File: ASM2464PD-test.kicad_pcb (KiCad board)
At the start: 2 copper layers, 34.6 x 22 mm, 19 parts, among them J1 USB_C_Receptacle, J2 Bus_M.2_Socket_M

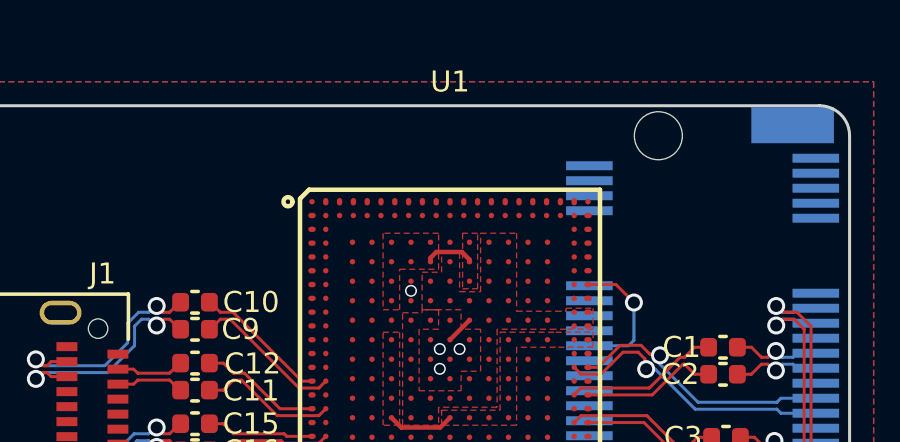
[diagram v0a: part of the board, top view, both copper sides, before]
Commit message: Labeled power rails, upgraded to KiCad 8
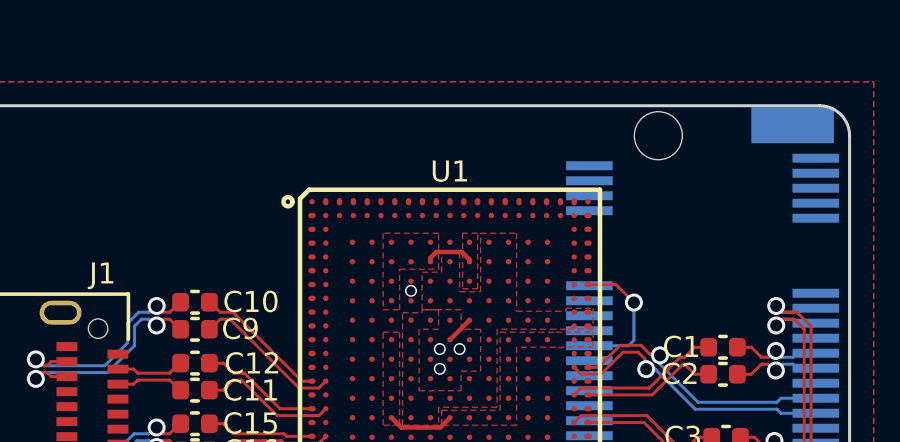
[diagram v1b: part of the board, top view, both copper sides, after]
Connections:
- net VCCH renamed 3.3V
- net VCCL renamed 1.8V
- net VDD renamed 1.05V
- U1 pad H5: unconnected-(U1C-VCCA33-PadH5) -> 3.3VA

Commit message: Updated symbol to match reference schematic
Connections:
- net 1.05V renamed 0.95V
- U1 pad G21: PERST# -> unconnected-(U1A-PERST0#-PadG21)

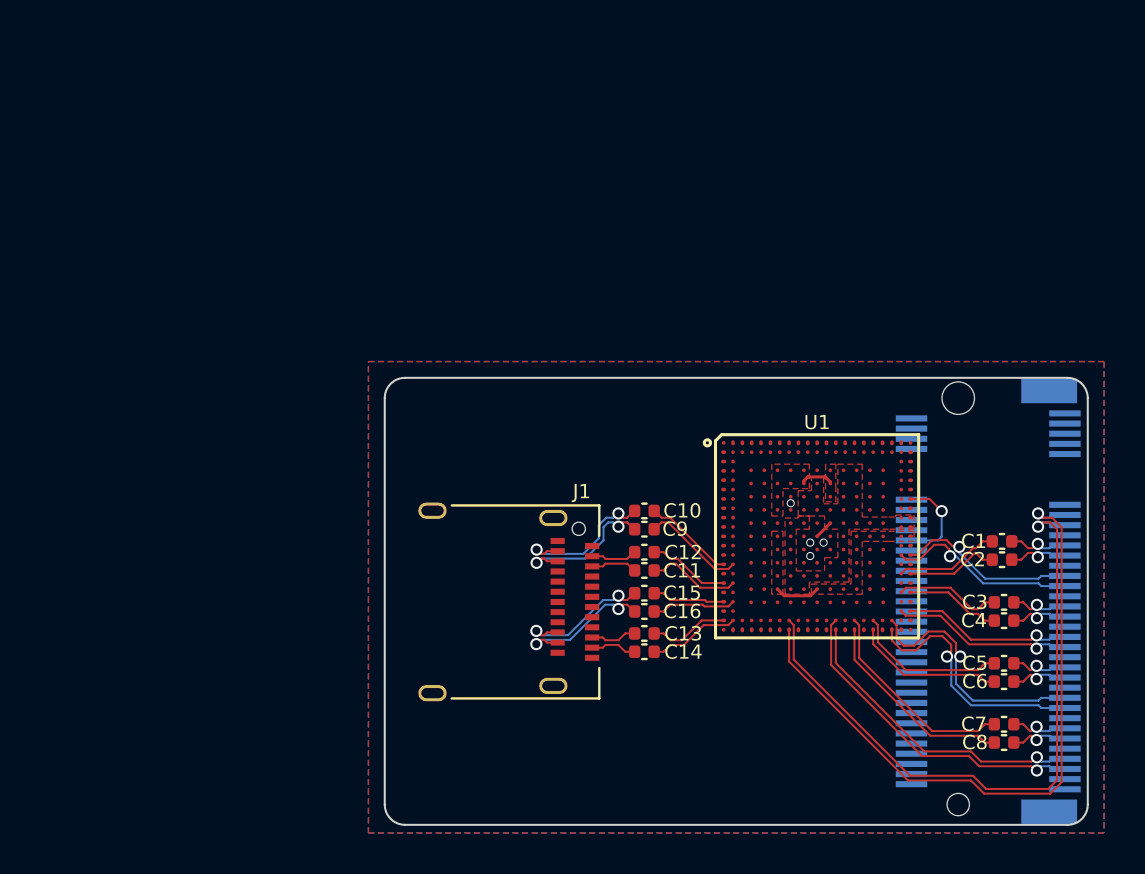
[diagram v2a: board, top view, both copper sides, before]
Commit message: Updated schematic and rerouted some stuff
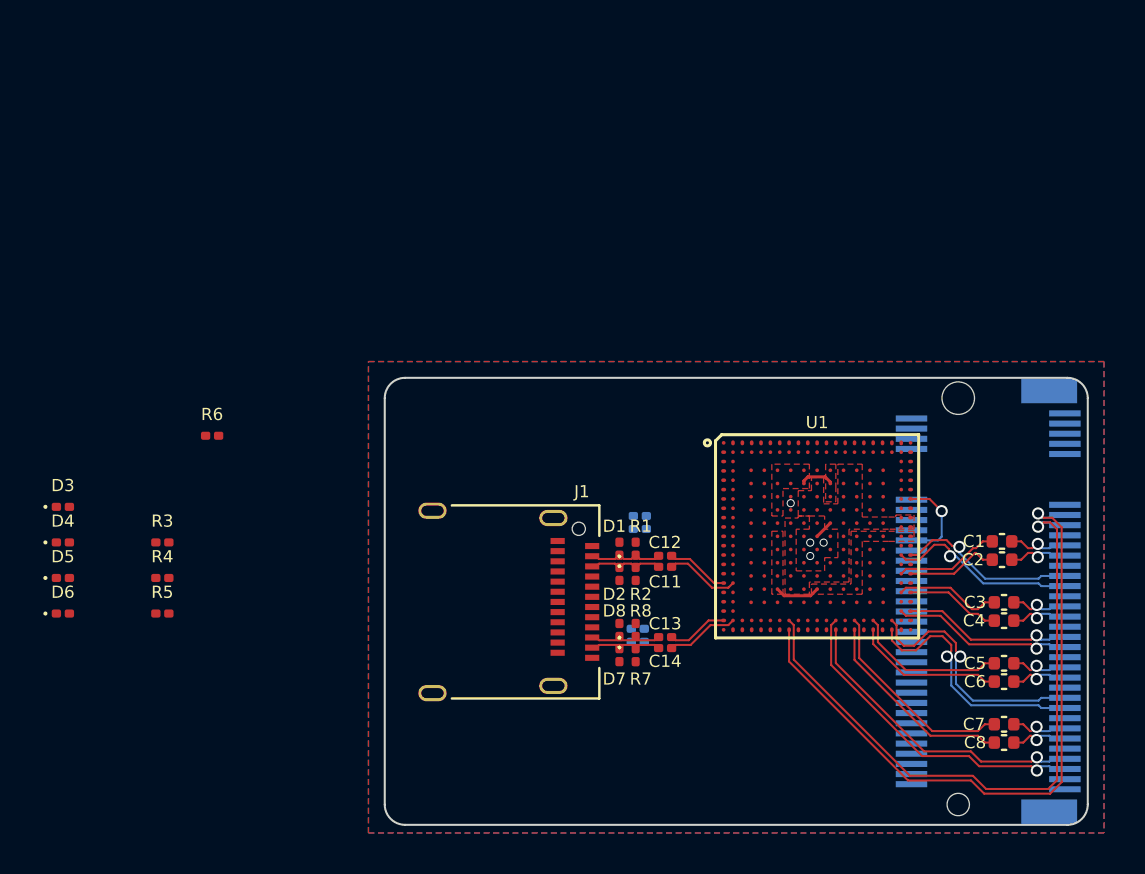
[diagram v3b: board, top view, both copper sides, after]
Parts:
- added D1: ~, Diode_SMD:D_0201_0603Metric, F.Cu at (57.0, 78.4)
- added D2: ~, Diode_SMD:D_0201_0603Metric, F.Cu at (57.0, 79.7)
- added D3: ~, Diode_SMD:D_0201_0603Metric, F.Cu at (29.6, 76.3)
- added D4: ~, Diode_SMD:D_0201_0603Metric, F.Cu at (29.6, 78.1)
- added D5: ~, Diode_SMD:D_0201_0603Metric, F.Cu at (29.6, 79.8)
- added D6: ~, Diode_SMD:D_0201_0603Metric, F.Cu at (29.6, 81.6)
- added D7: ~, Diode_SMD:D_0201_0603Metric, F.Cu at (57.0, 83.6)
- added D8: ~, Diode_SMD:D_0201_0603Metric, F.Cu at (57.0, 82.4)
- added R1: 220k, Resistor_SMD:R_0201_0603Metric, F.Cu at (57.8, 78.4)
- added R2: 220k, Resistor_SMD:R_0201_0603Metric, F.Cu at (57.8, 79.7)
- added R3: 220k, Resistor_SMD:R_0201_0603Metric, F.Cu at (34.5, 78.1)
- added R4: 220k, Resistor_SMD:R_0201_0603Metric, F.Cu at (34.5, 79.8)
- added R5: 220k, Resistor_SMD:R_0201_0603Metric, F.Cu at (34.5, 81.6)
- added R6: 220k, Resistor_SMD:R_0201_0603Metric, F.Cu at (36.9, 72.8)
- added R7: 220k, Resistor_SMD:R_0201_0603Metric, F.Cu at (57.8, 83.7)
- added R8: 220k, Resistor_SMD:R_0201_0603Metric, F.Cu at (57.8, 82.4)
- C10, C15, C16, C9: value 0.22u -> 0.33u; footprint Capacitor_SMD:C_0402_1005Metric -> Capacitor_SMD:C_0201_0603Metric; moved to B.Cu
- C11, C12, C13, C14: value 0.22u -> 0.33u; footprint Capacitor_SMD:C_0402_1005Metric -> Capacitor_SMD:C_0201_0603Metric
- moved C15 1.78 mm to (57.9, 82.3)
- moved C16 1.53 mm to (57.9, 83.0)
- moved C11 1.04 mm to (59.2, 79.3)
- moved C12 1.04 mm to (59.2, 78.8)
- moved C13 1.04 mm to (59.2, 82.8)
- moved C14 1.04 mm to (59.2, 83.3)
- moved C10 0.34 mm to (58.0, 76.8)
- moved C9 0.23 mm to (58.0, 77.4)
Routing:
- net /URX0_C-: track 7.52 -> 0.00 mm, vias 2 -> 0
- net /URX0_C+: track 7.52 -> 0.00 mm, vias 2 -> 0
- net /UTX1_C-: track 7.15 -> 0.00 mm, vias 2 -> 0
- net /UTX1_C+: track 7.15 -> 0.00 mm, vias 2 -> 0
- net URX0-: track 5.06 -> 0.00 mm
- net URX0+: track 4.51 -> 0.00 mm
- net UTX1+: track 4.15 -> 0.00 mm
- net UTX1-: track 3.59 -> 0.00 mm
- net /UTX0_C-: track 2.28 -> 3.70 mm
- net /UTX0_C+: track 2.28 -> 3.70 mm
- net /URX1_C-: track 2.28 -> 3.39 mm
- net /URX1_C+: track 2.28 -> 3.39 mm
- net URX1-: track 3.96 -> 3.03 mm
- net UTX0-: track 4.60 -> 3.67 mm
- net URX1+: track 4.52 -> 3.58 mm
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
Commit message: Added SPI flash, probably some more stuff, and made pcb 4-layer
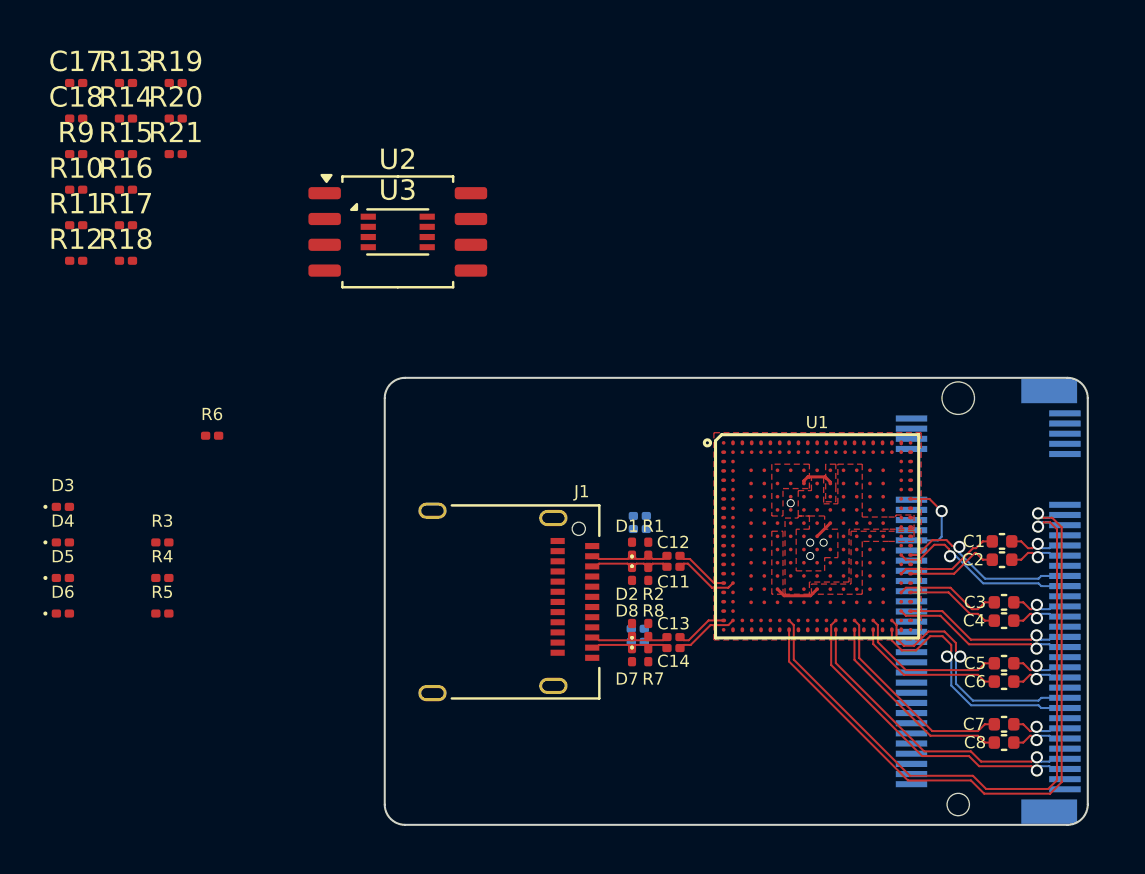
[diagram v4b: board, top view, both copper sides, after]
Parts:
- added C17: 1u, Capacitor_SMD:C_0201_0603Metric, F.Cu at (30.2, 55.5)
- added C18: 0.1u, Capacitor_SMD:C_0201_0603Metric, F.Cu at (30.2, 57.2)
- added R10: 0Ω, Resistor_SMD:R_0201_0603Metric, F.Cu at (30.2, 60.7)
- added R11: 0Ω, Resistor_SMD:R_0201_0603Metric, F.Cu at (30.2, 62.5)
- added R12: 0Ω, Resistor_SMD:R_0201_0603Metric, F.Cu at (30.2, 64.2)
- added R13: 0Ω, Resistor_SMD:R_0201_0603Metric, F.Cu at (32.7, 55.5)
- added R14: 0Ω, Resistor_SMD:R_0201_0603Metric, F.Cu at (32.7, 57.2)
- added R15: 4.7k, Resistor_SMD:R_0201_0603Metric, F.Cu at (32.7, 59.0)
- added R16: 10k, Resistor_SMD:R_0201_0603Metric, F.Cu at (32.7, 60.7)
- added R17: 4.7k, Resistor_SMD:R_0201_0603Metric, F.Cu at (32.7, 62.5)
- added R18: 4.7k, Resistor_SMD:R_0201_0603Metric, F.Cu at (32.7, 64.2)
- added R19: 0Ω, Resistor_SMD:R_0201_0603Metric, F.Cu at (35.1, 55.5)
- added R20: 0Ω, Resistor_SMD:R_0201_0603Metric, F.Cu at (35.1, 57.2)
- added R21: 0Ω, Resistor_SMD:R_0201_0603Metric, F.Cu at (35.1, 59.0)
- added R9: 0Ω, Resistor_SMD:R_0201_0603Metric, F.Cu at (30.2, 59.0)
- added U2: SPI_SOIC-8, Package_SO:SOIC-8_5.23x5.23mm_P1.27mm, F.Cu at (46.0, 62.8)
- added U3: SPI_DFN-8, Package_DFN_QFN:DFN-8-1EP_3x2mm_P0.5mm_EP1.3x1.5mm, F.Cu at (46.0, 62.8)
- moved D7 0.62 mm to (57.6, 83.7)
- moved D1 0.62 mm to (57.6, 78.4)
- moved D2 0.62 mm to (57.6, 79.7)
- moved D8 0.62 mm to (57.6, 82.4)
- moved R1 0.62 mm to (58.4, 78.4)
- moved R2 0.62 mm to (58.4, 79.7)
- moved R7 0.62 mm to (58.4, 83.7)
- moved R8 0.62 mm to (58.4, 82.4)
- moved C11 0.41 mm to (59.6, 79.3)
- moved C12 0.41 mm to (59.6, 78.8)
- moved C13 0.41 mm to (59.6, 82.8)
- moved C14 0.41 mm to (59.6, 83.3)
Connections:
- net 3.3V renamed +3.3V
- net 3.3VA renamed +3.3VA
- net Net-(J1-VBUS-PadA4) renamed +5V_VBUS
- J1 pad A5: CC1 -> /CC1_C
- J1 pad A6: USB2_D+ -> /USB2_C_D+
- J1 pad A7: USB2_D- -> /USB2_C_D-
- J1 pad A8: SBU1 -> /SBU1_C
- J1 pad B5: CC2 -> /CC2_C
- J1 pad B6: USB2_D+ -> /USB2_C_D+
- J1 pad B7: USB2_D- -> /USB2_C_D-
- J1 pad B8: SBU2 -> /SBU2_C
- J2 pad 50: PERST# -> Net-(J2-~{PERST})
- J2 pad 52: unconnected-(J2-~{CLKREQ}-Pad52) -> Net-(J2-~{CLKREQ})
- J2 pad 54: unconnected-(J2-~{PEWAKE}-Pad54) -> Net-(J2-~{PEWAKE})
- U1 pad A2: unconnected-(U1A-SPI_CS#-PadA2) -> SPI_CS#
- U1 pad A3: unconnected-(U1A-SPI_DO-PadA3) -> SPI_DO
- U1 pad A4: unconnected-(U1A-SPI_DI-PadA4) -> SPI_DI
- U1 pad A5: unconnected-(U1A-SPI_CLK-PadA5) -> SPI_CLK
- U1 pad G1: unconnected-(U1A-VBUS-PadG1) -> VBUS
- U1 pad G21: unconnected-(U1A-PERST0#-PadG21) -> PERST#
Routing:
- added copper zone on In1.Cu, net GND
- added copper zone on In2.Cu, net GND
- removed copper zone on B.Cu, net GND
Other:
- copper layers 2 -> 4

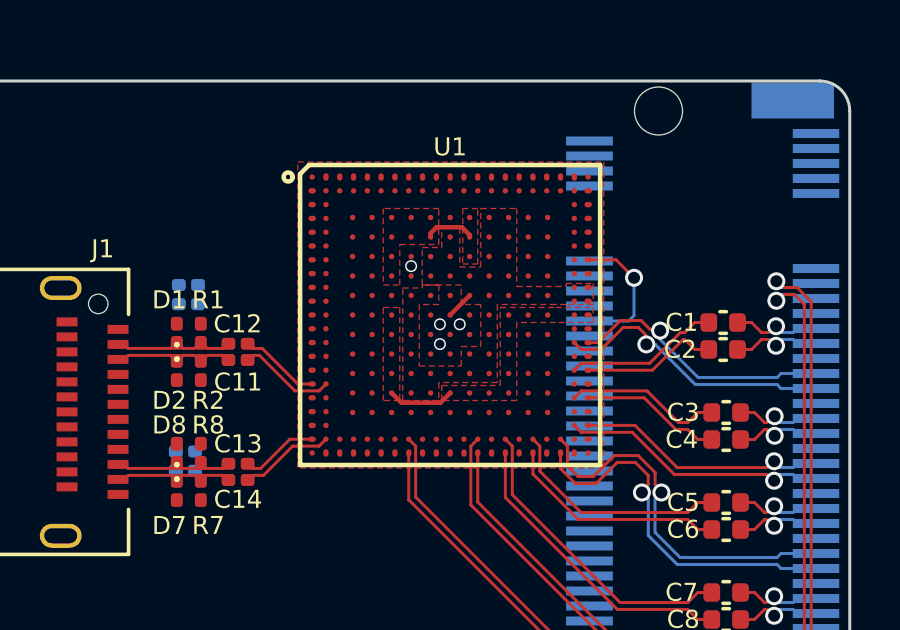
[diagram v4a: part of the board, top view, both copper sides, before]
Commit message: Added lots of power rail vias under chip
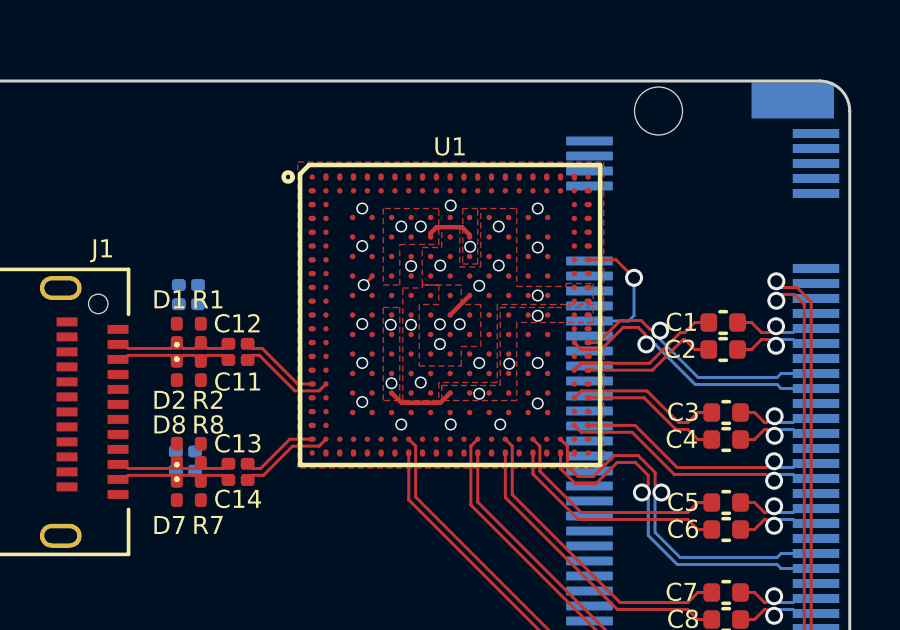
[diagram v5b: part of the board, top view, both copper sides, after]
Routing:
- net +3.3VA: track 0.00 -> 0.42 mm, vias 0 -> 1
- net GND: vias 4 -> 17
- net 1.8V: vias 0 -> 5
- net 0.95V: vias 0 -> 8
- net +3.3V: vias 0 -> 3

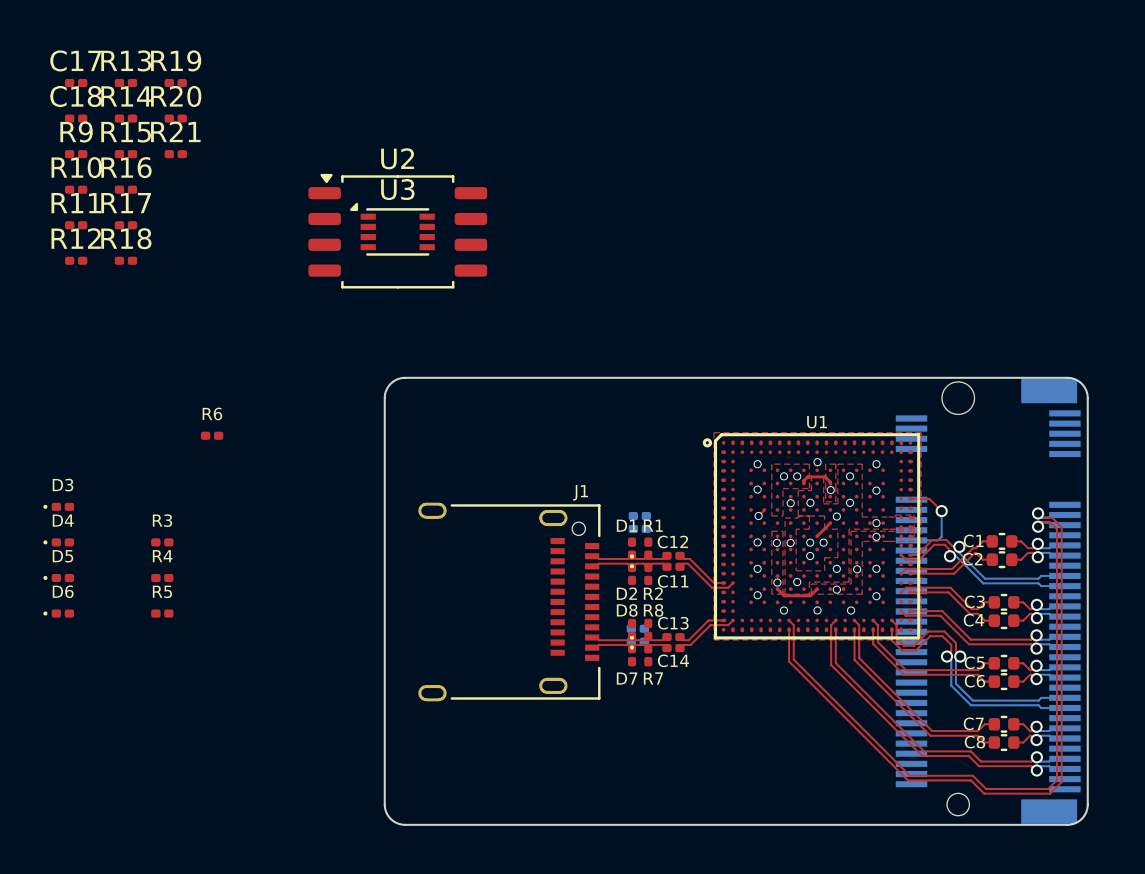
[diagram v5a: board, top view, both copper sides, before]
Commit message: reran the other 2 USB4 pairs too, placed esd stuff
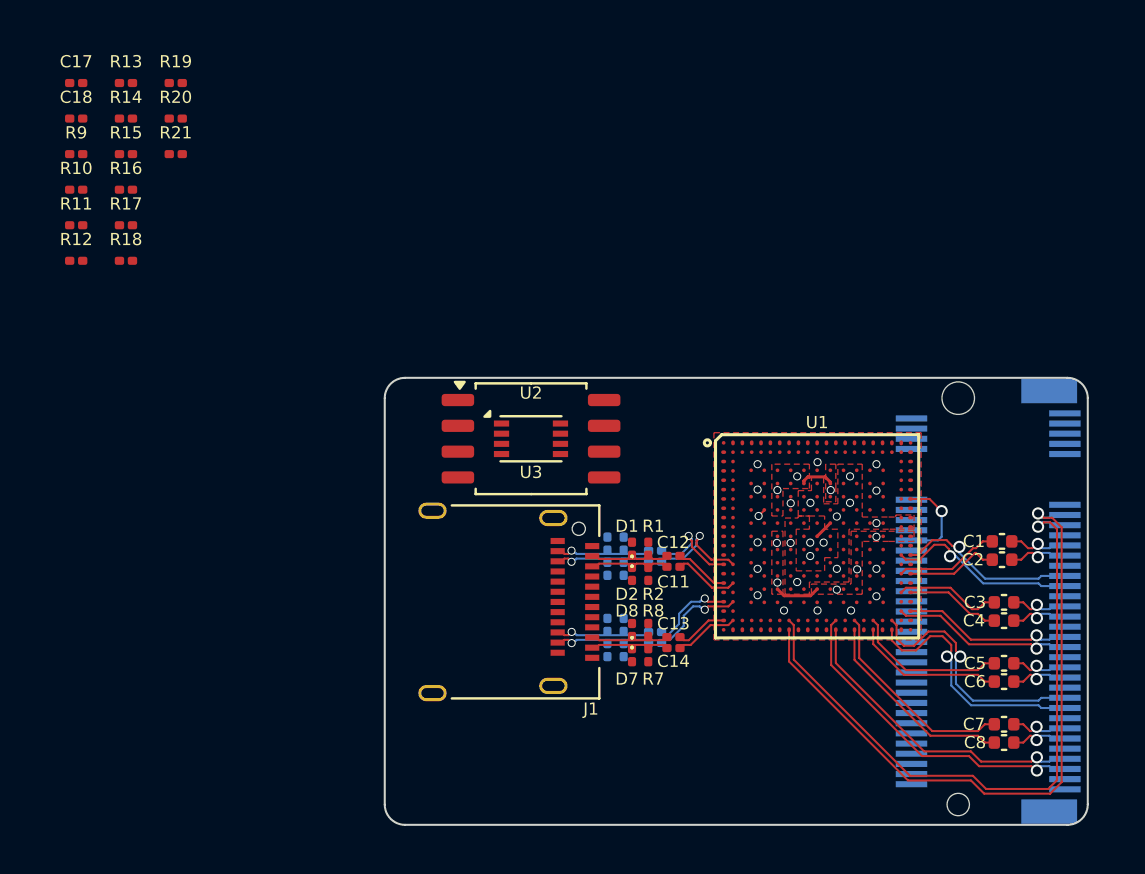
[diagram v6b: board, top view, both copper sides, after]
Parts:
- D3, D4, D5, D6, R3, R4, R5, R6: moved to B.Cu
- moved D5 27.0 mm to (56.4, 83.4), turned to -90 degrees
- moved D3 26.9 mm to (56.4, 78.2), turned to 90 degrees
- moved D4 26.8 mm to (56.4, 79.4), turned to -90 degrees
- moved D6 26.8 mm to (56.4, 82.2), turned to 90 degrees
- moved R5 22.8 mm to (57.2, 83.4), turned to -90 degrees
- moved R4 22.7 mm to (57.2, 79.4), turned to -90 degrees
- moved R3 22.7 mm to (57.2, 78.2), turned to 90 degrees
- moved R6 22.3 mm to (57.2, 82.2), turned to 90 degrees
- moved U2 12.1 mm to (52.6, 73.0)
- moved U3 12.1 mm to (52.6, 73.0)
- moved C10 1.87 mm to (58.7, 78.5)
- moved C9 1.78 mm to (58.7, 79.0)
- moved C15 0.86 mm to (58.7, 82.5)
- moved C16 0.85 mm to (58.7, 83.0)
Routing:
- net URX0-: track 0.00 -> 5.28 mm, vias 0 -> 1
- net UTX1+: track 0.00 -> 4.78 mm, vias 0 -> 1
- net /URX0_C-: track 0.00 -> 4.73 mm, vias 0 -> 1
- net /URX0_C+: track 0.00 -> 4.73 mm, vias 0 -> 1
- net /UTX1_C-: track 0.00 -> 4.73 mm, vias 0 -> 1
- net /UTX1_C+: track 0.00 -> 4.73 mm, vias 0 -> 1
- net URX0+: track 0.00 -> 4.73 mm, vias 0 -> 1
- net UTX1-: track 0.00 -> 4.23 mm, vias 0 -> 1

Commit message: Moved SPI flash footprint onto board
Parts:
- moved R19 43.0 mm to (72.8, 76.3), turned to -90 degrees
- moved R21 9.71 mm to (44.8, 58.0)
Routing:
- net PERST#: track 4.60 -> 1.47 mm, vias 1 -> 0
- net Net-(J2-~{PERST}): track 0.00 -> 2.67 mm, vias 0 -> 1
- net +3.3V: track 1.69 -> 4.32 mm
- net SPI_DO: track 0.00 -> 2.63 mm
- net SPI_CS#: track 0.00 -> 2.63 mm
- net GND: track 0.00 -> 2.62 mm
- net SPI_HOLD#: track 0.00 -> 2.31 mm
- net SPI_CLK: track 0.00 -> 2.31 mm
- net SPI_DI: track 0.00 -> 2.31 mm
- net SPI_WP#: track 0.00 -> 2.31 mm
